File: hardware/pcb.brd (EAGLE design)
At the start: 168.5 x 123.2 mm, 218 parts, among them IC1 LM386N-3, IC2 TL072P, IC6 7805

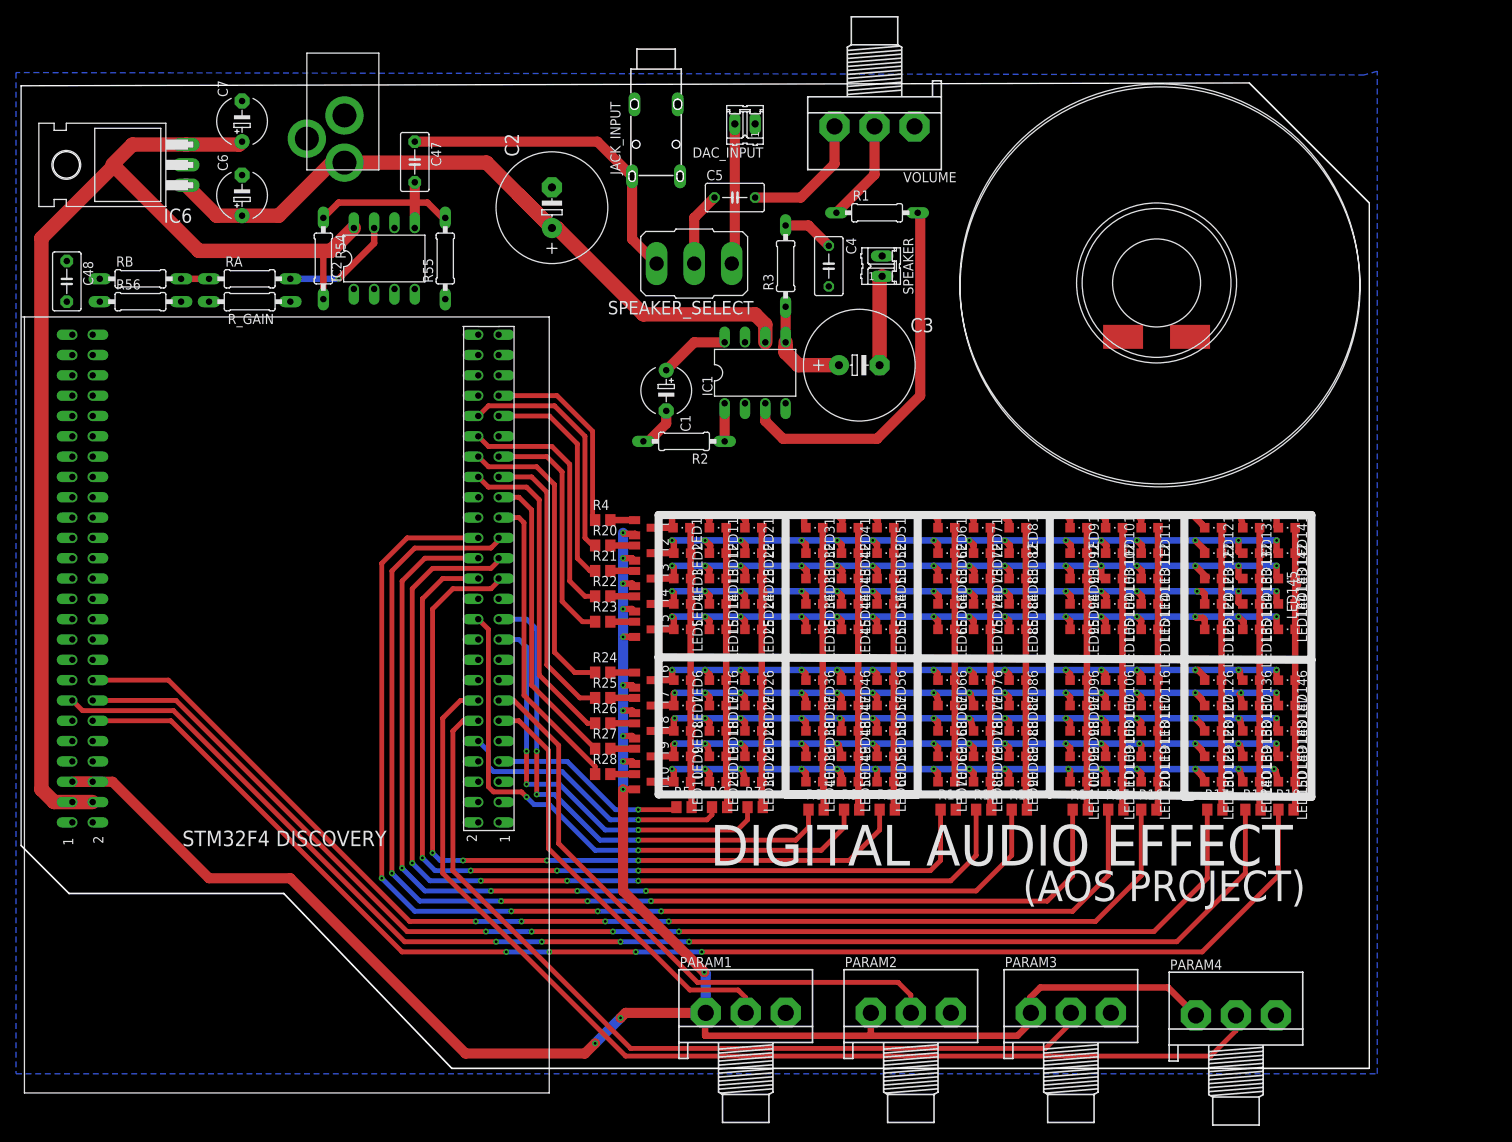
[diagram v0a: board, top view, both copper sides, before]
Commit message: DAC_Driver added
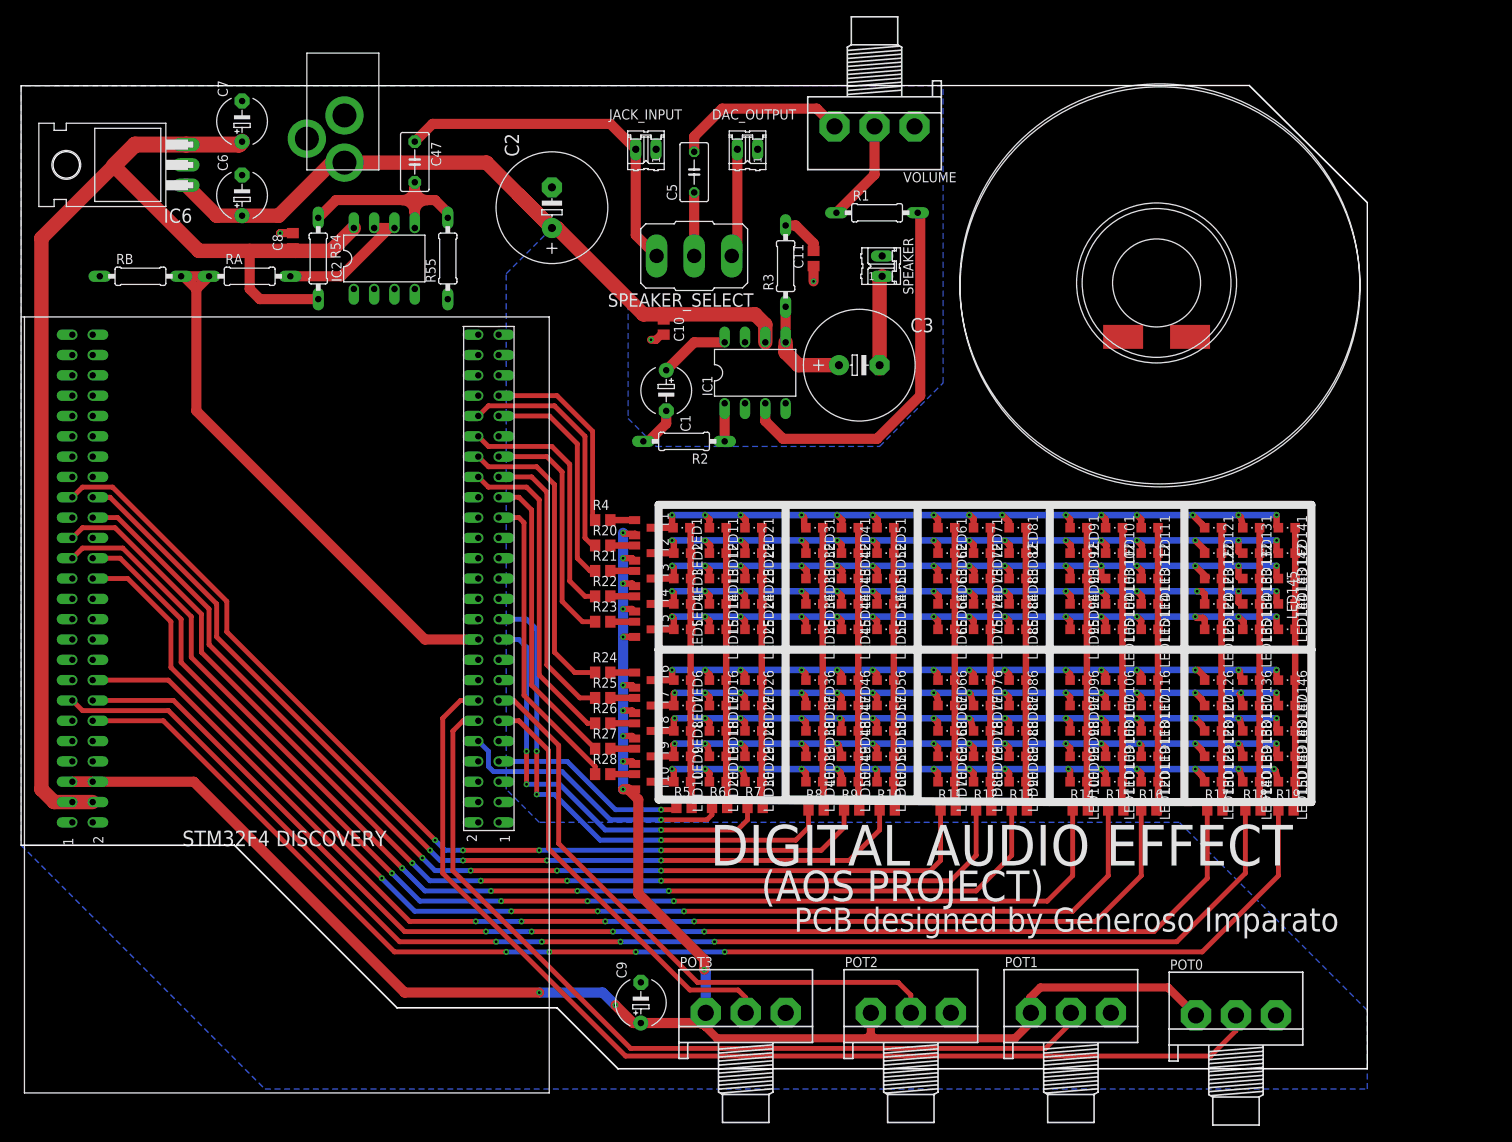
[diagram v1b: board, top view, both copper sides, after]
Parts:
- removed C4: 100n, rcl:C050-035X075
- removed C48: 470n, capacitor-wima:C5B3.5
- removed DAC_INPUT: (no value), con-amp-quick:02P
- removed R56: 110k, rcl:0207/10
- removed R_GAIN: 330k, rcl:0207/10
- added C10, C11, C8: 100n, rcl:C0805
- added C9: 100u, rcl:E5-6
- added DAC_OUTPUT: (no value), con-amp-quick:02P
- JACK_INPUT: value 1503_07 -> (none); device con-lumberg:1503_07 -> con-amp-quick:02P
- R10, R11, R12, R13, R14, R15, R16, R17, R18, R19, R5, R6, R7, R8, R9: value (none) -> 270
- R20, R21, R22, R23, R24, R25, R26, R27, R28, R4: value (none) -> 1.8k
- moved JACK_INPUT 7.73 mm to (78.1, 93.0), turned to 180 degrees
- moved C5 5.99 mm to (84.1, 90.2), turned to 90 degrees
- moved SPEAKER_SELECT 0.95 mm to (84.1, 79.7)
- moved R54 0.63 mm to (37.1, 79.4)
- moved RA 0.32 mm to (28.6, 77.2)
- moved RB 0.32 mm to (14.9, 77.2)
- moved R55 0.32 mm to (53.3, 79.4)
- renumbered PARAM1 to POT3, PARAM2 to POT2, PARAM3 to POT1, PARAM4 to POT0
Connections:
- removed net ADC_INPUT: RA.1, RB.2
- removed net N$38: C48.2, R56.1
- removed net N$85: IC2.6, R56.2, R_GAIN.2
- new net ADC_AUDIO_IN: BD1.PC4, RA.1, RB.2
- new net COL_5A: BD1.PB5
- net +3V3: now also C9.+
- net +5V: now also C8.1
- net COL_10: now also BD1.PD7; no longer BD1.PE11
- net COL_11: now also BD1.PB4; no longer BD1.PE12
- net COL_5: now also BD1.PD2; no longer BD1.PB0
- net COL_6: now also BD1.PD1; no longer BD1.PE7
- net COL_7: now also BD1.PD3; no longer BD1.PE8
- net COL_8: now also BD1.PD6; no longer BD1.PE9
- net COL_9: now also BD1.PB3; no longer BD1.PE10
- net GND: now also C10.2, C11.1, C8.2, C9.-, DAC_OUTPUT.1, JACK_INPUT.1; no longer C4.2, C48.1, DAC_INPUT.1, JACK_INPUT.2@1
- net GUITAR_BUFFER: now also IC2.6; no longer R_GAIN.1
- net N$27: now also JACK_INPUT.2; no longer JACK_INPUT.1
- net N$28: now also DAC_OUTPUT.2; no longer DAC_INPUT.2
- net N$36: now also C11.2; no longer C4.1
- net V+: now also C10.1
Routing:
- net ADC_AUDIO_IN: track 0.00 -> 70.9 mm
- net COL_5: track 72.6 -> 121.4 mm, vias 2 -> 4
- net COL_6: track 100.9 -> 123.7 mm
- net COL_7: track 112.7 -> 133.7 mm
- net COL_8: track 125.3 -> 141.6 mm
- net COL_9: track 131.5 -> 146.2 mm
- net N$77: track 22.5 -> 33.1 mm
- net +5V: track 148.6 -> 159.1 mm
- net +3V3: track 251.0 -> 257.0 mm
- net N$2: track 16.3 -> 21.8 mm
- net GND: track 0.00 -> 5.35 mm, vias 0 -> 3
- net GUITAR_BUFFER: track 14.2 -> 18.4 mm, vias 1 -> 0
- net N$28: track 17.6 -> 13.6 mm
- net COL_10: track 149.1 -> 153.0 mm
- net ADC_INPUT: track 3.81 -> 0.00 mm
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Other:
- board size 168.5 x 123.2 mm -> 168.3 x 122.9 mm
- board text added: "PCB designed by Generoso Imparato"

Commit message: PCB final (in production)
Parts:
- removed C11: 100n, rcl:C0805
- added C4: 100n, capacitor-wima:C5B3.5
- LED1, LED10, LED100, LED101, LED102, LED103, LED104, LED105, LED106, LED107, LED108, LED109, LED11, LED110, LED111, LED112, LED113, LED114, LED115, LED116, LED117, LED118, LED119, LED12, LED120, LED121, LED122, LED123, LED124, LED125, LED126, LED127, LED128, LED129, LED13, LED130, LED131, LED132, LED133, LED134, LED135, LED136, LED137, LED138, LED139, LED14, LED140, LED141, LED142, LED143, LED144, LED145, LED146, LED147, LED148, LED149, LED15, LED150, LED16, LED17, LED18, LED19, LED2, LED20, LED21, LED22, LED23, LED24, LED25, LED26, LED27, LED28, LED29, LED3, LED30, LED31, LED32, LED33, LED34, LED35, LED36, LED37, LED38, LED39, LED4, LED40, LED41, LED42, LED43, LED44, LED45, LED46, LED47, LED48, LED49, LED5, LED50, LED51, LED52, LED53, LED54, LED55, LED56, LED57, LED58, LED59, LED6, LED60, LED61, LED62, LED63, LED64, LED65, LED66, LED67, LED68, LED69, LED7, LED70, LED71, LED72, LED73, LED74, LED75, LED76, LED77, LED78, LED79, LED8, LED80, LED81, LED82, LED83, LED84, LED85, LED86, LED87, LED88, LED89, LED9, LED90, LED91, LED92, LED93, LED94, LED95, LED96, LED97, LED98, LED99: value (none) -> led 0805
- SPEAKER_SELECT: device switch:M9040P -> adafruit:EG1218
- T1, T10, T2, T3, T4, T5, T6, T7, T8, T9: value (none) -> PNP SOT23
- moved C10 0.64 mm to (80.3, 71.4)
- moved SPEAKER_SELECT 0.63 mm to (84.1, 79.1), turned to 180 degrees
- moved R5 0.32 mm to (82.9, 10.5)
- moved R6 0.32 mm to (87.3, 10.5)
- moved R7 0.32 mm to (91.8, 10.5)
- renumbered JACK_INPUT to ADC_INPUT
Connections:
- net GND: now also C4.1; no longer C11.1
- net N$27: now also SPEAKER_SELECT.S; no longer SPEAKER_SELECT.3
- net N$28: now also SPEAKER_SELECT.O; no longer SPEAKER_SELECT.1
- net N$36: now also C4.2; no longer C11.2
- net N$37: now also SPEAKER_SELECT.P; no longer SPEAKER_SELECT.2
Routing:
- net GND: track 5.35 -> 2.86 mm, vias 3 -> 2
- net N$27: track 44.9 -> 47.0 mm
- net N$28: track 13.6 -> 15.2 mm
- net N$36: track 5.37 -> 6.40 mm
- net N$37: track 7.94 -> 8.57 mm
